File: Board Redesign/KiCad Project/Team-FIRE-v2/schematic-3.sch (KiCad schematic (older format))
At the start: 2 parts

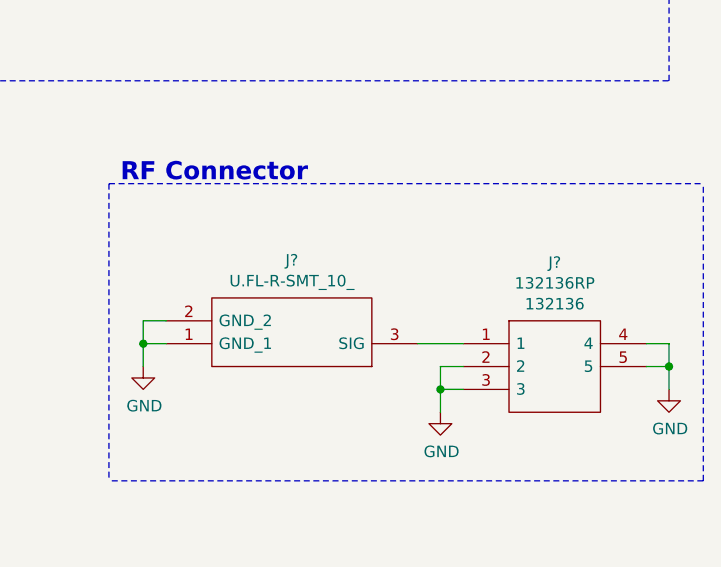
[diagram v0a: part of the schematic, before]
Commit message: Minor label fix on RF connector
- Removed display of "value" field on RF connector, changed display to MPN on both
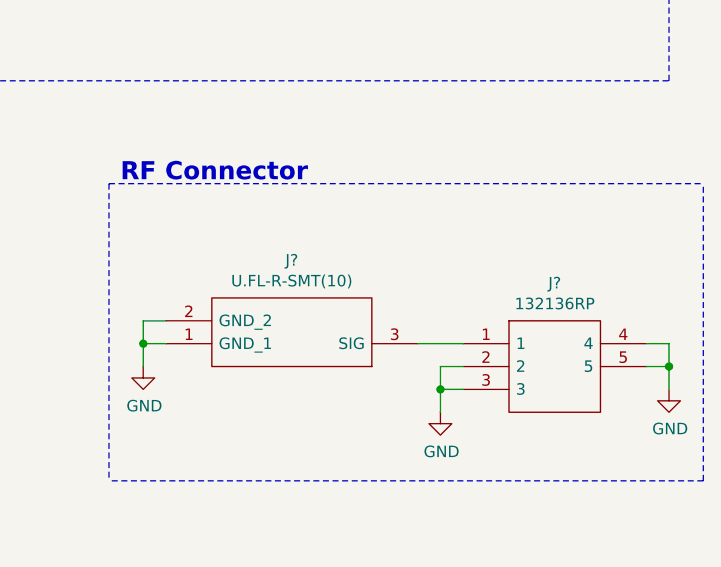
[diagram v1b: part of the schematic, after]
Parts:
- J?: MPN (none) -> U.FL-R-SMT(10); Manufacturer_Part_Number U.FL-R-SMT(10) -> (none)
- J?: MPN 132136 -> 132136RP; Manufacturer_Part_Number 132136RP -> (none)
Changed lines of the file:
@@
 P 9600 5450
 F 0 "J?" H 10150 5085 50  0000 C CNN
-F 1 "U.FL-R-SMT_10_" H 10150 5176 50  0000 C CNN
+F 1 "U.FL-R-SMT_10_" H 10150 5086 50  0001 C CNN
 F 2 "UFLRSMT10" H 10550 5550 50  0001 L CNN
 F 3 "https://media.digikey.com/pdf/Data%20Sheets/Hirose%20PDFs/UFL%20Series.pdf" H 10550 5450 50  0001 L CNN
@@
 F 5 "1.25" H 10550 5250 50  0001 L CNN "Height"
 F 6 "Hirose" H 10550 5150 50  0001 L CNN "Manufacturer_Name"
-F 7 "U.FL-R-SMT(10)" H 10550 5050 50  0001 L CNN "Manufacturer_Part_Number"
+F 7 "U.FL-R-SMT(10)" H 10150 5176 50  0000 C CNN "MPN"
 F 8 "798-U.FL-R-SMT10" H 10550 4950 50  0001 L CNN "Mouser Part Number"
 F 9 "https://www.mouser.com/Search/Refine.aspx?Keyword=798-U.FL-R-SMT10" H 10550 4850 50  0001 L CNN "Mouser Price/Stock"
@@
 U 1 1 5EA604BA
 P 9800 5450
-F 0 "J?" H 10200 5805 50  0000 C CNN
-F 1 "132136RP" H 10200 5714 50  0000 C CNN
+F 0 "J?" H 10200 5715 50  0000 C CNN
+F 1 "132136RP" H 10200 5714 50  0001 C CNN
 F 2 "132136RP" H 10450 5550 50  0001 L CNN
 F 3 "https://componentsearchengine.com/Datasheets/2/132136RP.pdf" H 10450 5450 50  0001 L CNN
@@
 F 5 "9.86" H 10450 5250 50  0001 L CNN "Height"
 F 6 "Amphenol" H 10450 5150 50  0001 L CNN "Manufacturer_Name"
-F 7 "132136RP" H 10450 5050 50  0001 L CNN "Manufacturer_Part_Number"
-F 8 "523-132136RP" H 10450 4950 50  0001 L CNN "Mouser Part Number"
-F 9 "https://www.mouser.com/Search/Refine.aspx?Keyword=523-132136RP" H 10450 4850 50  0001 L CNN "Mouser Price/Stock"
-F 10 "70032830" H 10450 4550 50  0001 L CNN "Allied_Number"
-F 11 "https://www.alliedelec.com/amphenolrf-132136rp/70032830/" H 10450 4450 50  0001 L CNN "Allied Price/Stock"
-F 12 "132136" H 10200 5623 50  0000 C CNN "MPN"
+F 7 "523-132136RP" H 10450 4950 50  0001 L CNN "Mouser Part Number"
+F 8 "https://www.mouser.com/Search/Refine.aspx?Keyword=523-132136RP" H 10450 4850 50  0001 L CNN "Mouser Price/Stock"
+F 9 "70032830" H 10450 4550 50  0001 L CNN "Allied_Number"
+F 10 "https://www.alliedelec.com/amphenolrf-132136rp/70032830/" H 10450 4450 50  0001 L CNN "Allied Price/Stock"
+F 11 "132136RP" H 10200 5624 50  0000 C CNN "MPN"
 	1    9800 5450
 	1    0    0    -1

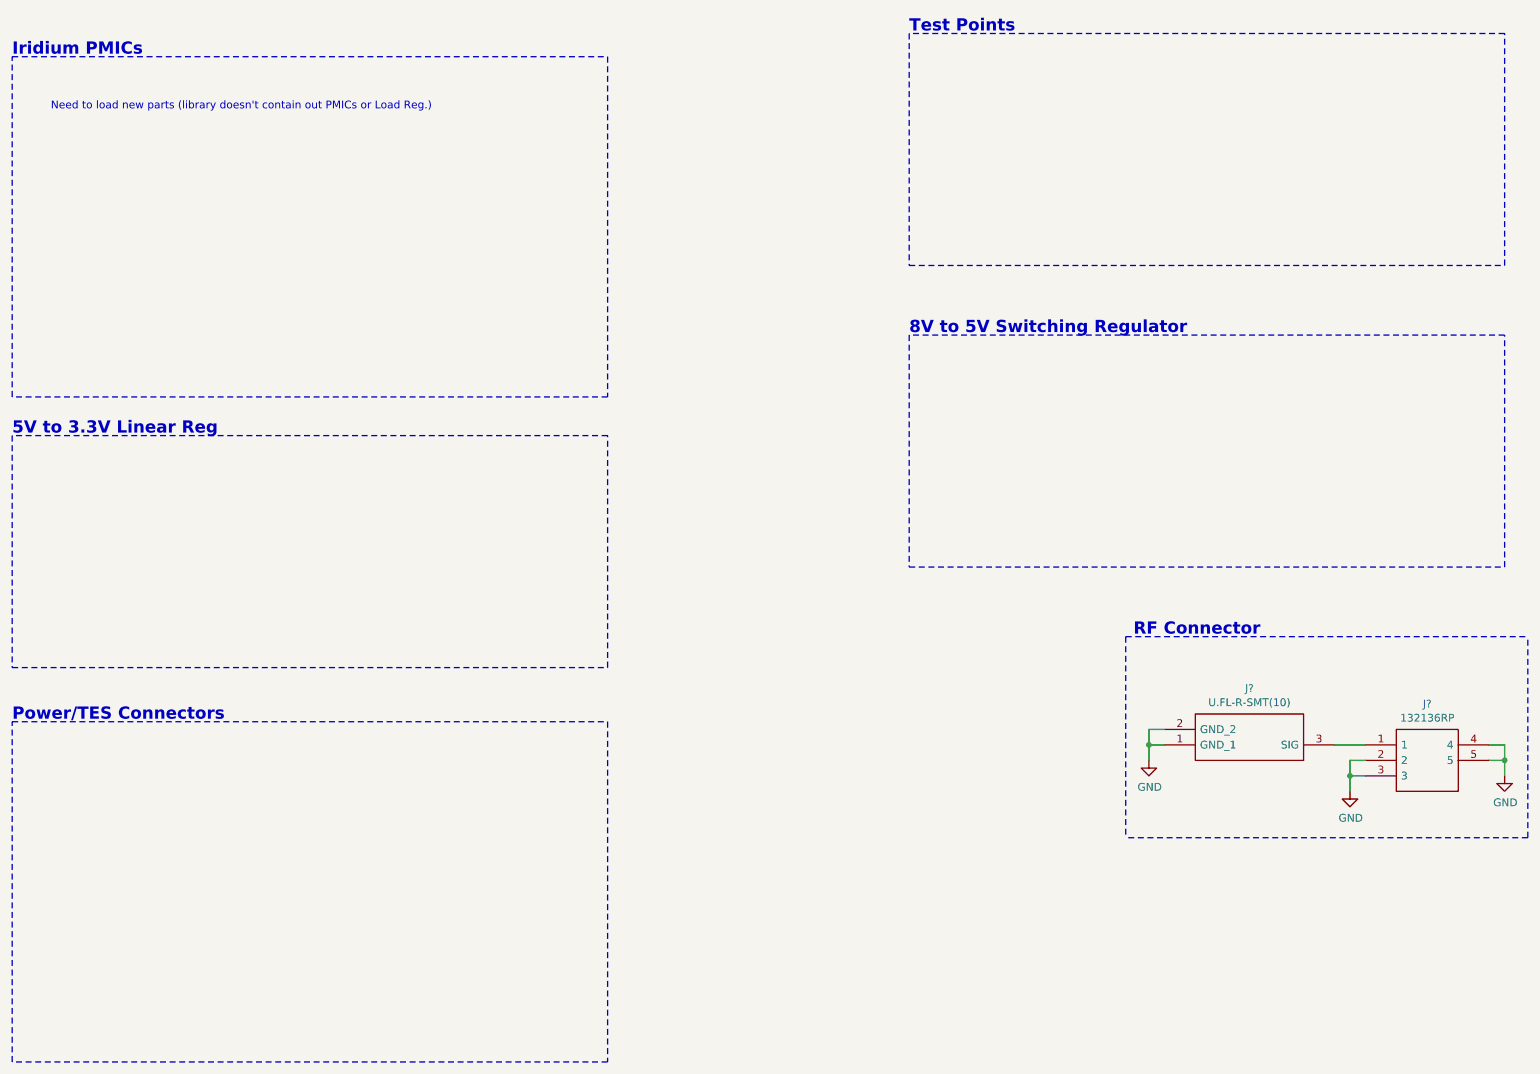
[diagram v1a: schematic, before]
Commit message: Added PMIC part, 3.3V lin reg part, and buck converter + testpoint part
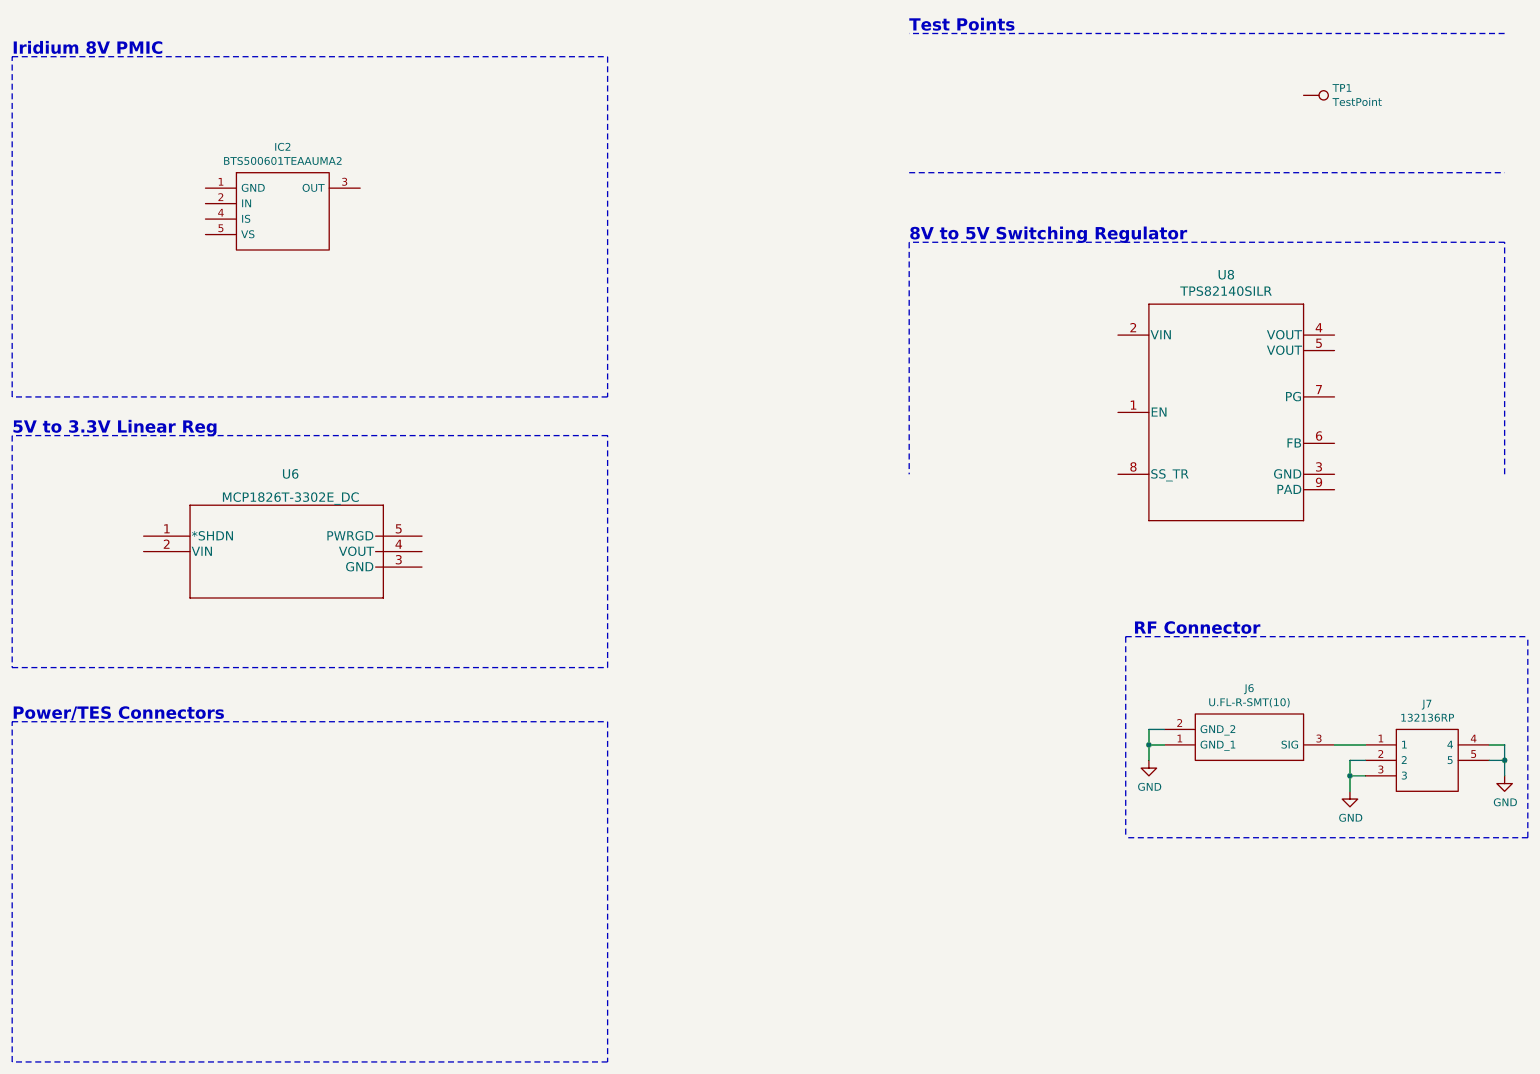
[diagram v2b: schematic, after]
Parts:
- added IC2: BTS500601TEAAUMA2, BTS500601TEAAUMA2, symbol BTS500601TEAAUMA2:BTS500601TEAAUMA2
- added TP1: TestPoint, symbol Connector:TestPoint
- added U6: MCP1826T-3302E_DC, SOT-223_5MC_MCH, symbol 5_to_3.3_linreg:MCP1826T-3302E_DC
- added U8: TPS82140SILR, SIL0008D_SMD, symbol sw_reg:TPS82140SILR
- gave numbers to parts that had none: 2
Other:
- note added: "Iridium 8V PMIC"
- note removed: "Iridium PMICs"
- note removed: "Need to load new parts (library doesn't contain out PMICs or Load Reg.)"
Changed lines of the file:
@@
 EESchema Schematic File Version 4
-LIBS:Team-FIRE-v2-cache
 EELAYER 30 0
 EELAYER END
@@
 Test Points
 Text Notes 1050 1000 0    79   ~ 16
-Iridium PMICs
+Iridium 8V PMIC
 Wire Notes Line
 	1050 5300 4900 5300
@@
 	4900 1000 4900 3200
 Wire Notes Line
-	4900 3200 1050 3200
-Wire Notes Line
 	1050 3200 1050 1000
 Wire Notes Line
 	1050 1000 4900 1000
 Wire Notes Line
-	1050 3450 1050 4950
-Wire Notes Line
-	1050 4950 4900 4950
-Wire Notes Line
-	4900 4950 4900 3450
-Wire Notes Line
-	4900 3450 1050 3450
-Text Notes 1050 3450 0    79   ~ 16
-5V to 3.3V Linear Reg
-Text Notes 1300 1350 0    50   ~ 0
-Need to load new parts (library doesn't contain out PMICs or Load Reg.)
-Wire Notes Line
-	6850 2800 6850 4300
-Wire Notes Line
-	6850 4300 10700 4300
-Wire Notes Line
-	10700 4300 10700 2800
-Wire Notes Line
-	10700 2800 6850 2800
-Text Notes 6850 2800 0    79   ~ 16
+	6850 2200 6850 3700
+Wire Notes Line
+	10700 3700 10700 2200
+Wire Notes Line
+	10700 2200 6850 2200
+Text Notes 6850 2200 0    79   ~ 16
 8V to 5V Switching Regulator
 Wire Notes Line
-	6850 850  6850 2350
-Wire Notes Line
-	6850 2350 10700 2350
-Wire Notes Line
-	10700 2350 10700 850
+	6850 1750 10700 1750
 Wire Notes Line
 	10700 850  6850 850
@@
 	10700 5550 10700 5650
 $Comp
-L power:GND #PWR?
+L power:GND #PWR0152
 U 1 1 5EA5E592
 P 10700 5650
-F 0 "#PWR?" H 10700 5400 50  0001 C CNN
+F 0 "#PWR0152" H 10700 5400 50  0001 C CNN
 F 1 "GND" H 10705 5477 50  0000 C CNN
 F 2 "" H 10700 5650 50  0001 C CNN
@@
 $EndComp
 $Comp
-L power:GND #PWR?
+L power:GND #PWR0153
 U 1 1 5EA5E7F7
 P 9700 5750
-F 0 "#PWR?" H 9700 5500 50  0001 C CNN
+F 0 "#PWR0153" H 9700 5500 50  0001 C CNN
 F 1 "GND" H 9705 5577 50  0000 C CNN
 F 2 "" H 9700 5750 50  0001 C CNN
@@
 $EndComp
 $Comp
-L Team-FIRE:U.FL-R-SMT_10_ J?
+L Team-FIRE:U.FL-R-SMT_10_ J6
 U 1 1 5EA5F3F4
 P 9600 5450
-F 0 "J?" H 10150 5085 50  0000 C CNN
+F 0 "J6" H 10150 5085 50  0000 C CNN
 F 1 "U.FL-R-SMT_10_" H 10150 5086 50  0001 C CNN
 F 2 "UFLRSMT10" H 10550 5550 50  0001 L CNN
@@
 $EndComp
 $Comp
-L Team-FIRE:132136RP J?
+L Team-FIRE:132136RP J7
 U 1 1 5EA604BA
 P 9800 5450
-F 0 "J?" H 10200 5715 50  0000 C CNN
+F 0 "J7" H 10200 5715 50  0000 C CNN
 F 1 "132136RP" H 10200 5714 50  0001 C CNN
 F 2 "132136RP" H 10450 5550 50  0001 L CNN
@@
 	9600 5450 9800 5450
 $Comp
-L power:GND #PWR?
+L power:GND #PWR0154
 U 1 1 5EA632DA
 P 8400 5550
-F 0 "#PWR?" H 8400 5300 50  0001 C CNN
+F 0 "#PWR0154" H 8400 5300 50  0001 C CNN
 F 1 "GND" H 8405 5377 50  0000 C CNN
 F 2 "" H 8400 5550 50  0001 C CNN
@@
 Wire Notes Line
 	10850 6050 8250 6050
+Wire Notes Line
+	4900 3200 1050 3200
+Text Notes 1050 3450 0    79   ~ 16
+5V to 3.3V Linear Reg
+Wire Notes Line
+	4900 3450 1050 3450
+Wire Notes Line
+	4900 4950 4900 3450
+Wire Notes Line
+	1050 4950 4900 4950
+Wire Notes Line
+	1050 3450 1050 4950
+$Comp
+L BTS500601TEAAUMA2:BTS500601TEAAUMA2 IC2
+U 1 1 5EA814BB
+P 2300 1850
+F 0 "IC2" H 2800 2115 50  0000 C CNN
+F 1 "BTS500601TEAAUMA2" H 2800 2024 50  0000 C CNN
+F 2 "BTS500601TEAAUMA2" H 3150 1950 50  0001 L CNN
+F 3 "https://www.infineon.com/dgdl/Infineon-BTS50060-1TEA-DS-v01_02-EN.pdf?fileId=5546d46259d9a4bf015a8518bd3f7781" H 3150 1850 50  0001 L CNN
+F 4 "INFINEON - BTS500601TEAAUMA2 - Power Load Switch, AEC-Q100, High Side, 1 Output, 13.5 V, 60 A/0.0068 ohm out, TO-252-5" H 3150 1750 50  0001 L CNN "Description"
+F 5 "2.4" H 3150 1650 50  0001 L CNN "Height"
+F 6 "Infineon" H 3150 1550 50  0001 L CNN "Manufacturer_Name"
+F 7 "BTS500601TEAAUMA2" H 3150 1450 50  0001 L CNN "Manufacturer_Part_Number"
+F 8 "726-BTS500601TEAAUMA" H 3150 1350 50  0001 L CNN "Mouser Part Number"
+F 9 "https://www.mouser.com/Search/Refine.aspx?Keyword=726-BTS500601TEAAUMA" H 3150 1250 50  0001 L CNN "Mouser Price/Stock"
+F 10 "" H 3150 1150 50  0001 L CNN "RS Part Number"
+F 11 "" H 3150 1050 50  0001 L CNN "RS Price/Stock"
+	1    2300 1850
+	1    0    0    -1
+$EndComp
+$Comp
+L 5_to_3.3_linreg:MCP1826T-3302E_DC U6
+U 1 1 5EA82E51
+P 1900 4100
+F 0 "U6" H 2850 4500 60  0000 C CNN
+F 1 "MCP1826T-3302E_DC" H 2850 4350 60  0000 C CNN
+F 2 "SOT-223_5MC_MCH" H 3200 4340 60  0001 C CNN
+F 3 "" H 1900 4100 60  0000 C CNN
+	1    1900 4100
+	1    0    0    -1
+$EndComp
+$Comp
+L Connector:TestPoint TP1
+U 1 1 5EA85276
+P 9400 1250
+F 0 "TP1" V 9354 1438 50  0000 L CNN
+F 1 "TestPoint" V 9445 1438 50  0000 L CNN
+F 2 "" H 9600 1250 50  0001 C CNN
+F 3 "~" H 9600 1250 50  0001 C CNN
+	1    9400 1250
+	0    1    1    0
+$EndComp
+$Comp
+L sw_reg:TPS82140SILR U8
+U 1 1 5EA86302
+P 8900 3300
+F 0 "U8" H 8900 4188 60  0000 C CNN
+F 1 "TPS82140SILR" H 8900 4082 60  0000 C CNN
+F 2 "SIL0008D_SMD" H 8900 3240 60  0001 C CNN
+F 3 "" H 8900 3300 60  0000 C CNN
+	1    8900 3300
+	1    0    0    -1
+$EndComp
 $EndSCHEMATC
